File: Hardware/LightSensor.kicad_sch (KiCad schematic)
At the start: 2 parts, among them U4 LTR-303ALS-01

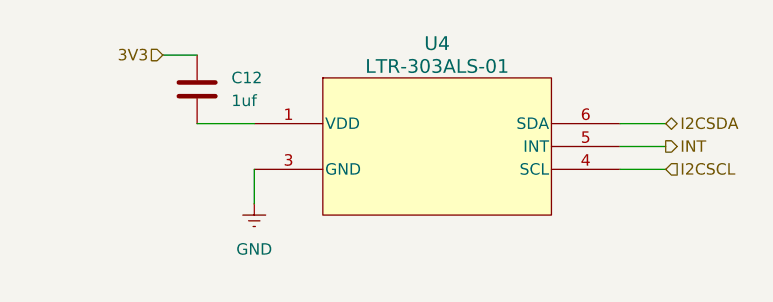
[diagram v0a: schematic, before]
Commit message: Use tags for nets, apply netgroups, mess around in pcb view
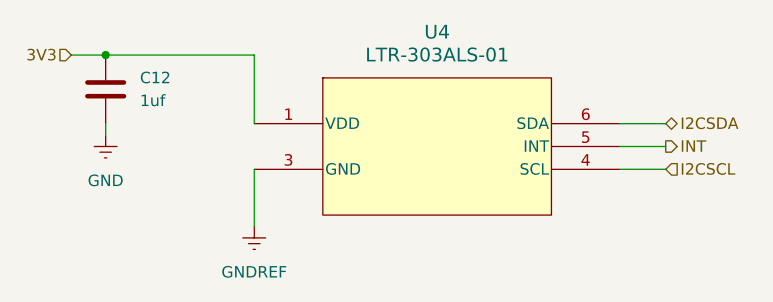
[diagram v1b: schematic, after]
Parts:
- C12: footprint (none) -> Capacitor_SMD:C_0201_0603Metric
- U4: footprint Snapeda:LTR-303ALS-01_LTO -> Snapeda:LTR-329ALS-01_LTO
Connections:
- net 3V3: now also U4.1 (VDD)
- net GND: now also C12.2; no longer U4.3 (GND)
- new net GNDREF: U4.3 (GND)
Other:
- moved on the sheet: C12
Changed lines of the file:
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@@
 	(generator_version "8.0")
 	(paper "A4")
+	(junction
+		(at 80.01 76.2)
+		(diameter 0)
+		(color 0 0 0 0)
+	)
 	(wire
 		(pts
@@
 	(wire
 		(pts
-			(xy 96.52 88.9) (xy 96.52 92.71)
+			(xy 80.01 85.09) (xy 80.01 83.82)
 		)
 		(stroke
@@
 	(wire
 		(pts
-			(xy 90.17 83.82) (xy 96.52 83.82)
-		)
-		(stroke
-			(width 0)
-			(type default)
-		)
-	)
-	(wire
-		(pts
-			(xy 86.36 76.2) (xy 90.17 76.2)
+			(xy 80.01 76.2) (xy 96.52 76.2)
+		)
+		(stroke
+			(width 0)
+			(type default)
+		)
+	)
+	(wire
+		(pts
+			(xy 96.52 76.2) (xy 96.52 83.82)
+		)
+		(stroke
+			(width 0)
+			(type default)
+		)
+	)
+	(wire
+		(pts
+			(xy 96.52 88.9) (xy 96.52 95.25)
+		)
+		(stroke
+			(width 0)
+			(type default)
+		)
+	)
+	(wire
+		(pts
+			(xy 76.2 76.2) (xy 80.01 76.2)
 		)
 		(stroke
@@
 	(hierarchical_label "3V3"
 		(shape input)
-		(at 86.36 76.2 180)
+		(at 76.2 76.2 180)
 		(fields_autoplaced yes)
 		(effects
@@
 	(symbol
 		(lib_id "Peanut:LTR-303ALS-01")
-		(at 96.52 85.09 0)
+		(at 96.52 83.82 0)
 		(unit 1)
 		(exclude_from_sim no)
@@
 		(fields_autoplaced yes)
 		(property "Reference" "U4"
-			(at 116.84 74.93 0)
+			(at 116.84 73.66 0)
 			(effects
 				(font
@@
 		)
 		(property "Value" "LTR-303ALS-01"
-			(at 116.84 77.47 0)
+			(at 116.84 76.2 0)
 			(effects
 				(font
@@
 			)
 		)
-		(property "Footprint" "Snapeda:LTR-303ALS-01_LTO"
-			(at 117.602 102.108 0)
+		(property "Footprint" "Snapeda:LTR-329ALS-01_LTO"
+			(at 117.602 100.838 0)
 			(effects
 				(font
@@
 		)
 		(property "Datasheet" "LTR-303ALS-01"
-			(at 117.348 96.52 0)
+			(at 117.348 95.25 0)
 			(effects
 				(font
@@
 		)
 		(property "Description" ""
-			(at 96.52 83.82 0)
+			(at 96.52 82.55 0)
 			(effects
 				(font
@@
 	(symbol
 		(lib_id "Peanut:GND")
-		(at 96.52 92.71 0)
+		(at 80.01 85.09 0)
 		(unit 1)
 		(exclude_from_sim no)
@@
 		(dnp no)
 		(fields_autoplaced yes)
-		(property "Reference" "#PWR015"
-			(at 96.52 99.06 0)
+		(property "Reference" "#PWR018"
+			(at 80.01 91.44 0)
 			(effects
 				(font
@@
 		)
 		(property "Value" "GND"
-			(at 96.52 97.79 0)
+			(at 80.01 90.17 0)
 			(effects
 				(font
@@
 		)
 		(property "Footprint" ""
-			(at 96.52 92.71 0)
+			(at 80.01 85.09 0)
 			(effects
 				(font
@@
 		)
 		(property "Datasheet" ""
-			(at 96.52 92.71 0)
+			(at 80.01 85.09 0)
 			(effects
 				(font
@@
 		)
 		(property "Description" "Power symbol creates a global label with name \"GNDREF\" , reference supply ground"
-			(at 96.52 92.71 0)
+			(at 80.01 85.09 0)
 			(effects
 				(font
@@
 			(project "Peanut"
 				(path "/298ef215-2a76-4225-b9ba-26c57869f278/0e93c783-48c0-427a-ae2f-e1cfd30fce47"
-					(reference "#PWR015")
+					(reference "#PWR018")
 					(unit 1)
 				)
@@
 	)
 	(symbol
-		(lib_id "Device:C")
-		(at 90.17 80.01 0)
+		(lib_id "PartsLib:GNDREF")
+		(at 96.52 95.25 0)
 		(unit 1)
 		(exclude_from_sim no)
@@
 		(dnp no)
 		(fields_autoplaced yes)
+		(property "Reference" "#PWR019"
+			(at 96.52 101.6 0)
+			(effects
+				(font
+					(size 1.27 1.27)
+				)
+				(hide yes)
+			)
+		)
+		(property "Value" "GNDREF"
+			(at 96.52 100.33 0)
+			(effects
+				(font
+					(size 1.27 1.27)
+				)
+			)
+		)
+		(property "Footprint" ""
+			(at 96.52 95.25 0)
+			(effects
+				(font
+					(size 1.27 1.27)
+				)
+				(hide yes)
+			)
+		)
+		(property "Datasheet" ""
+			(at 96.52 95.25 0)
+			(effects
+				(font
+					(size 1.27 1.27)
+				)
+				(hide yes)
+			)
+		)
+		(property "Description" "Power symbol creates a global label with name \"GNDREF\" , reference supply ground"
+			(at 96.52 95.25 0)
+			(effects
+				(font
+					(size 1.27 1.27)
+				)
+				(hide yes)
+			)
+		)
+		(pin "1"
+		)
+		(instances
+			(project "Peanut"
+				(path "/298ef215-2a76-4225-b9ba-26c57869f278/0e93c783-48c0-427a-ae2f-e1cfd30fce47"
+					(reference "#PWR019")
+					(unit 1)
+				)
+			)
+		)
+	)
+	(symbol
+		(lib_id "Device:C")
+		(at 80.01 80.01 0)
+		(unit 1)
+		(exclude_from_sim no)
+		(in_bom yes)
+		(on_board yes)
+		(dnp no)
+		(fields_autoplaced yes)
 		(property "Reference" "C12"
-			(at 93.98 78.7399 0)
+			(at 83.82 78.7399 0)
 			(effects
 				(font
@@
 		)
 		(property "Value" "1uf"
-			(at 93.98 81.2799 0)
+			(at 83.82 81.2799 0)
 			(effects
 				(font
@@
 			)
 		)
-		(property "Footprint" ""
-			(at 91.1352 83.82 0)
+		(property "Footprint" "Capacitor_SMD:C_0201_0603Metric"
+			(at 80.9752 83.82 0)
 			(effects
 				(font
@@
 		)
 		(property "Datasheet" "~"
-			(at 90.17 80.01 0)
+			(at 80.01 80.01 0)
 			(effects
 				(font
@@
 		)
 		(property "Description" "Unpolarized capacitor"
-			(at 90.17 80.01 0)
-			(effects
-				(font
+			(at 80.01 80.01 0)
+			(effects
+				(font

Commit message: Use Peanut symbols, fix ERC errors, progress on DAC & Pressure
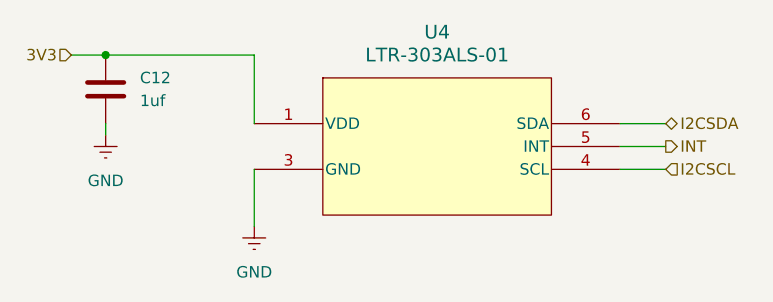
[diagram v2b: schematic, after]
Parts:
- U4: footprint Snapeda:LTR-329ALS-01_LTO -> Peanut:LTR-308ALS-01_LTO; Manufacturer (none) -> Lite-On
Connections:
- net GNDREF is gone; now on net GND: U4.3 (GND)
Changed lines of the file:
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@@
 			)
 		)
-		(property "Footprint" "Snapeda:LTR-329ALS-01_LTO"
+		(property "Footprint" "Peanut:LTR-308ALS-01_LTO"
 			(at 117.602 100.838 0)
 			(effects
@@
 		(property "Description" ""
 			(at 96.52 82.55 0)
+			(effects
+				(font
+					(size 1.27 1.27)
+				)
+				(hide yes)
+			)
+		)
+		(property "Manufacturer" "Lite-On"
+			(at 96.52 83.82 0)
 			(effects
 				(font
@@
 	)
 	(symbol
-		(lib_id "PartsLib:GNDREF")
+		(lib_id "Peanut:GND")
 		(at 96.52 95.25 0)
 		(unit 1)
@@
 			)
 		)
-		(property "Value" "GNDREF"
+		(property "Value" "GND"
 			(at 96.52 100.33 0)
 			(effects
@@
 			)
 		)
-		(property "Description" "Power symbol creates a global label with name \"GNDREF\" , reference supply ground"
-			(at 96.52 95.25 0)
+		(property "Description" ""
+			(at 96.52 103.886 0)
 			(effects
 				(font

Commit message: Fully wired board!
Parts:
- C12: footprint Capacitor_SMD:C_0201_0603Metric -> Resistor_SMD:R_01005_0402Metric; symbol Device:C -> Peanut:C
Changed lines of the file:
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@@
 	)
 	(symbol
-		(lib_id "Device:C")
+		(lib_id "Peanut:C")
 		(at 80.01 80.01 0)
 		(unit 1)
@@
 			)
 		)
-		(property "Footprint" "Capacitor_SMD:C_0201_0603Metric"
+		(property "Footprint" "Resistor_SMD:R_01005_0402Metric"
 			(at 80.9752 83.82 0)
 			(effects

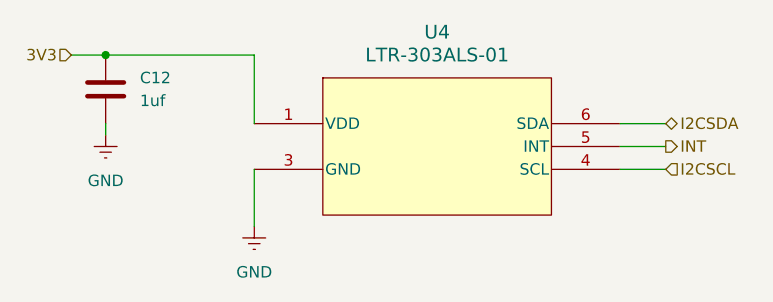
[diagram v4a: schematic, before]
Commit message: Initial OS architecture, and updated PCB work After a joint planning session, designed and architected OS structure: ``` src/ |- os: Audio, Accelerometer, Humidity, etc |- drivers: I2C interfaces, per-chip ```
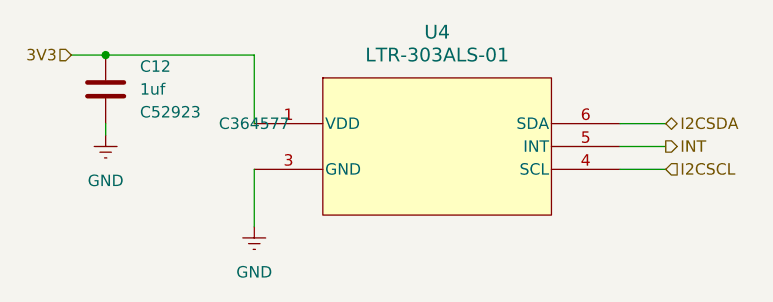
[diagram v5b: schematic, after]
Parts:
- C12: footprint Resistor_SMD:R_01005_0402Metric -> Capacitor_SMD:C_0402_1005Metric; symbol Peanut:C -> Peanut:C 1uF; LCSC (none) -> C52923
- U4: LCSC (none) -> C364577
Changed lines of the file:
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@@
+			)
+		)
+		(property "LCSC" "C364577"
+			(at 96.52 83.82 0)
+			(effects
+				(font
+					(size 1.27 1.27)
+				)
 			)
 		)
@@
 	)
 	(symbol
-		(lib_id "Peanut:C")
+		(lib_id "Peanut:C 1uF")
 		(at 80.01 80.01 0)
 		(unit 1)
@@
 		(fields_autoplaced yes)
 		(property "Reference" "C12"
-			(at 83.82 78.7399 0)
+			(at 83.82 77.4699 0)
 			(effects
 				(font
@@
 		)
 		(property "Value" "1uf"
-			(at 83.82 81.2799 0)
+			(at 83.82 80.0099 0)
 			(effects
 				(font
@@
 			)
 		)
-		(property "Footprint" "Resistor_SMD:R_01005_0402Metric"
+		(property "Footprint" "Capacitor_SMD:C_0402_1005Metric"
 			(at 80.9752 83.82 0)
 			(effects
@@
 			)
 		)
+		(property "LCSC" "C52923"
+			(at 83.82 82.5499 0)
+			(effects
+				(font
+					(size 1.27 1.27)
+				)
+				(justify left)
+			)
+		)
